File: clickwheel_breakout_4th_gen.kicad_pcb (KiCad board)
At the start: 2 copper layers, 55.5 x 98.2 mm, 7 parts, among them J1 SFV8R-2STE1HLF, J2 SFV14R-2STE1HLF, J3 SFV8R-2STE1HLF, J4 SFV14R-2STE1HLF, J5 Conn_02x08_Odd_Even, J6 Conn_02x14_Odd_Even, J7 USB_C_Receptacle_USB2.0

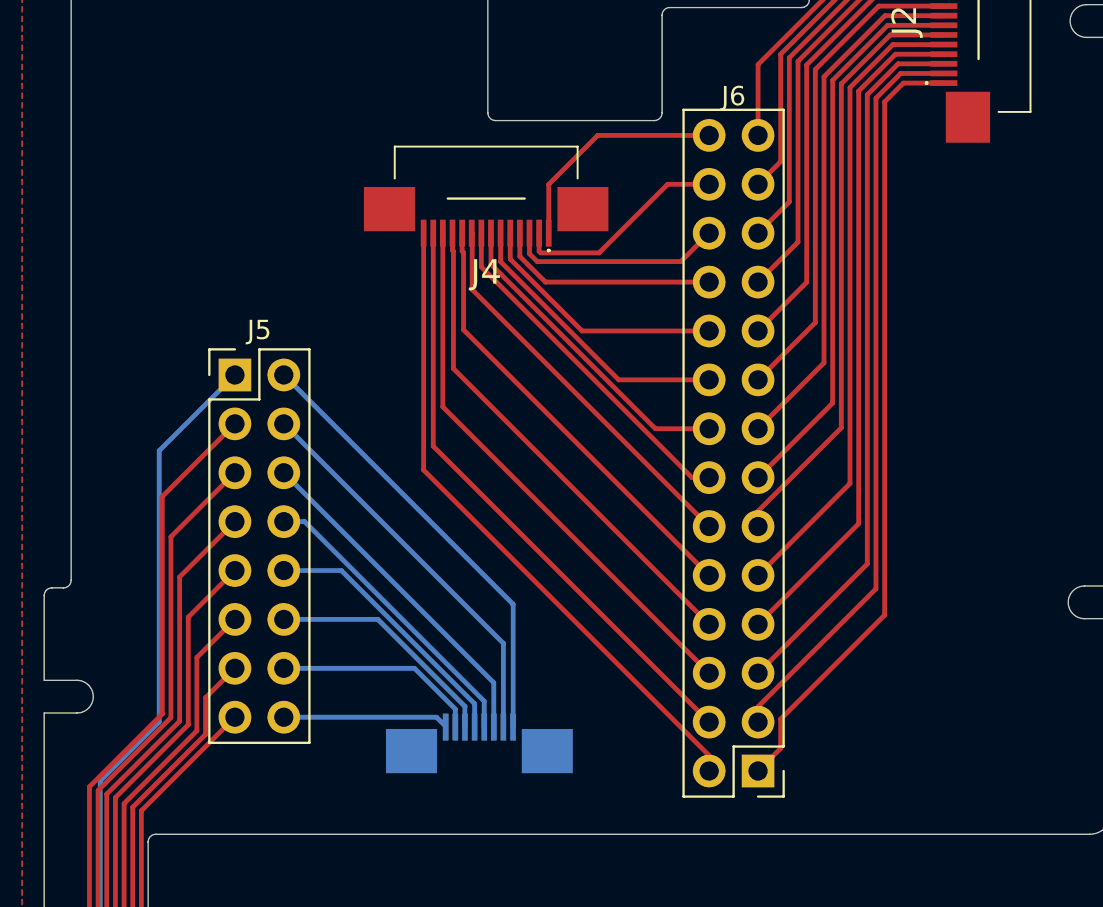
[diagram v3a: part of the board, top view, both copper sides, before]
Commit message: Add known headphone signal names with silkscreen
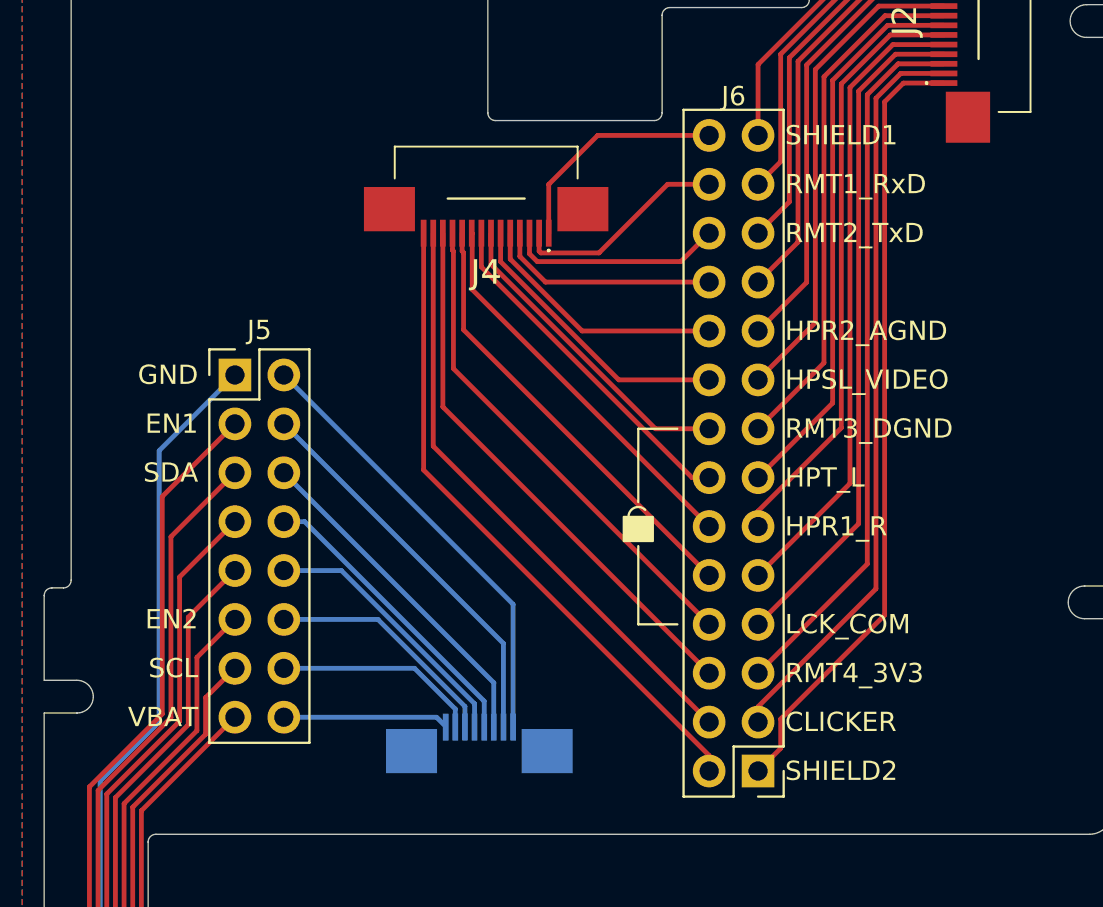
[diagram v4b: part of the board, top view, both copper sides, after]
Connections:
- net GND renamed Net-(J7-PadA1)
- net HP_1 renamed HP_SHIELD2
- net HP_10 renamed HP_HPR2_AGND
- net HP_10MB renamed HP_HPR2_AGNDMB
- net HP_12 renamed HP_RMT2_TxD
- net HP_12MB renamed HP_RMT2_TxDMB
- net HP_13 renamed HP_RMT1_RxD
- net HP_13MB renamed HP_RMT1_RxDMB
- net HP_14 renamed HP_SHIELD1
- net HP_14MB renamed HP_SHIELD1MB
- net HP_1MB renamed HP_SHIELD2MB
- net HP_2 renamed HP_CLICKER
- net HP_2MB renamed HP_CLICKERMB
- net HP_3 renamed HP_RMT4_3V3
- net HP_3MB renamed HP_RMT4_3V3MB
- net HP_4 renamed HP_LCK_COM
- net HP_4MB renamed HP_LCK_COMMB
- net HP_6 renamed HP_HPR1_R
- net HP_6MB renamed HP_HPR1_RMB
- net HP_7 renamed HP_HPT_L
- net HP_7MB renamed HP_HPT_LMB
- net HP_8 renamed HP_RMT3_DGND
- net HP_8MB renamed HP_RMT3_DGNDMB
- net HP_9 renamed HP_HPSL_VIDEO
- net HP_9MB renamed HP_HPSL_VIDEOMB
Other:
- board text added: "CLICKER"
- board text added: "Connect LCK_COM to DGND to unlock controls"
- board text added: "HPR1_R"
- board text added: "HPR2_AGND"
- board text added: "HPSL_VIDEO"
- board text added: "HPT_L"
- board text added: "LCK_COM"
- board text added: "RMT1_RxD"
- board text added: "RMT2_TxD"
- board text added: "RMT3_DGND"
- board text added: "RMT4_3V3"
- board text added: "SHIELD1"
- board text added: "SHIELD2"

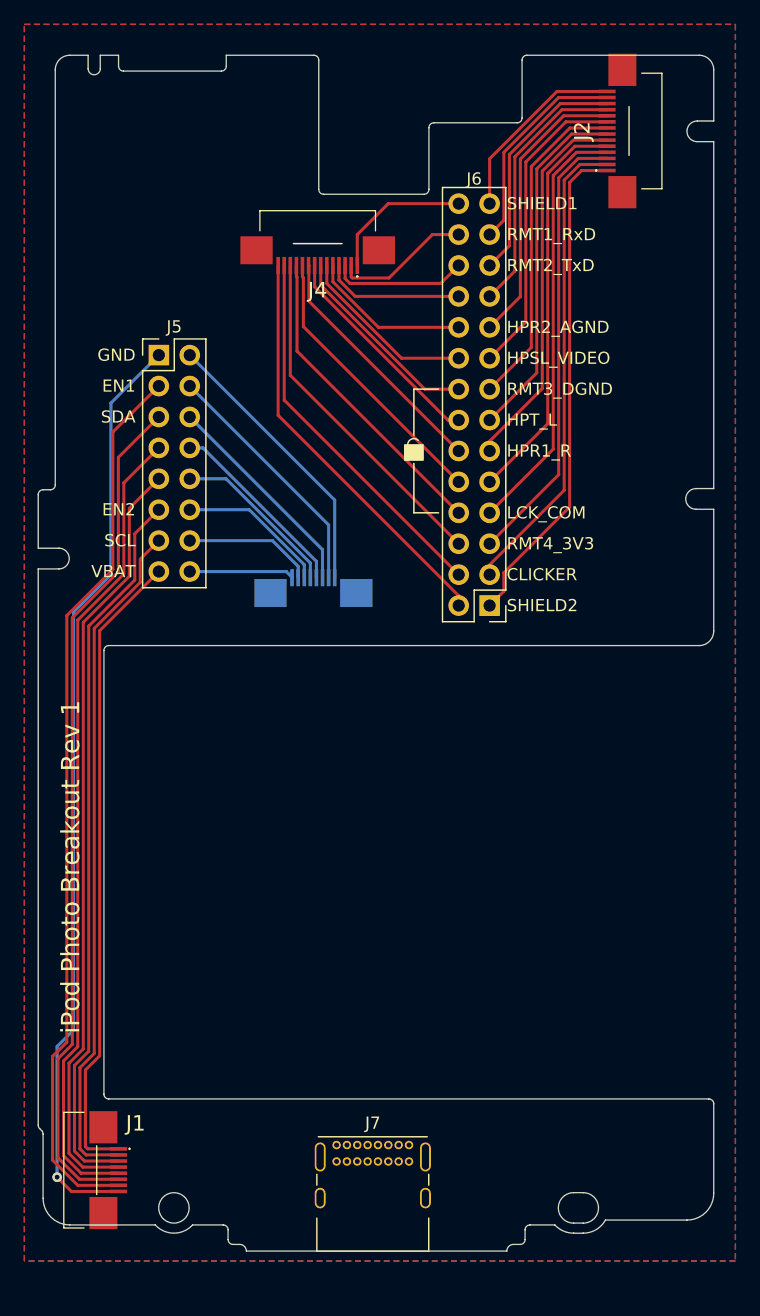
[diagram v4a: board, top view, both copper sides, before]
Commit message: kicad: update to kicad 6
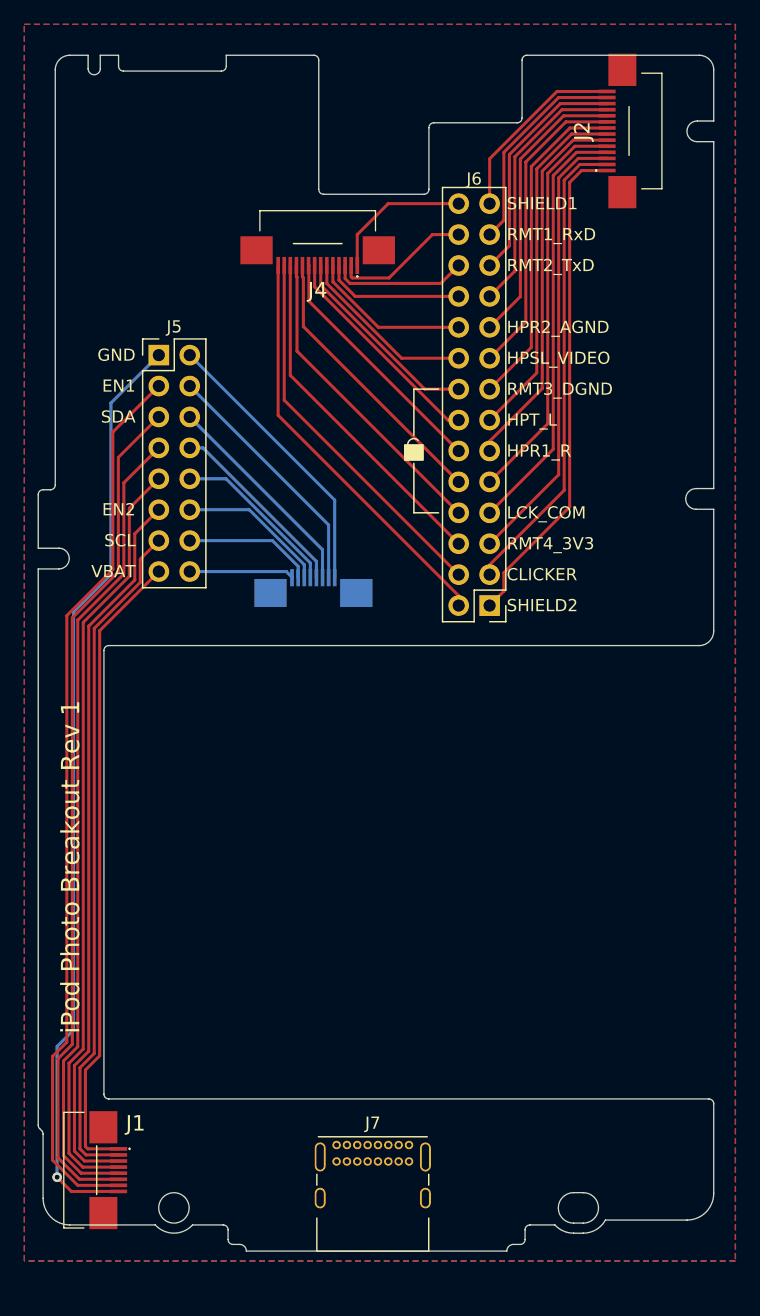
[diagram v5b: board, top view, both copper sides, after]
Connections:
- J1 pad M1: Net-(J1-PadM1) -> unconnected-(J1-PadM1)
- J1 pad M2: Net-(J1-PadM2) -> unconnected-(J1-PadM2)
- J2 pad M1: Net-(J2-PadM1) -> unconnected-(J2-PadM1)
- J2 pad M2: Net-(J2-PadM2) -> unconnected-(J2-PadM2)
- J3 pad M1: Net-(J3-PadM1) -> unconnected-(J3-PadM1)
- J3 pad M2: Net-(J3-PadM2) -> unconnected-(J3-PadM2)
- J4 pad M1: Net-(J4-PadM1) -> unconnected-(J4-PadM1)
- J4 pad M2: Net-(J4-PadM2) -> unconnected-(J4-PadM2)
- J7 pad A1: Net-(J7-PadA1) -> unconnected-(J7-PadA1)
- J7 pad A12: Net-(J7-PadA1) -> unconnected-(J7-PadA1)
- J7 pad A4: Net-(J7-PadA4) -> unconnected-(J7-PadA4)
- J7 pad A5: Net-(J7-PadA5) -> unconnected-(J7-PadA5)
- J7 pad A6: Net-(J7-PadA6) -> unconnected-(J7-PadA6)
- J7 pad A7: Net-(J7-PadA7) -> unconnected-(J7-PadA7)
- J7 pad A8: Net-(J7-PadA8) -> unconnected-(J7-PadA8)
- J7 pad A9: Net-(J7-PadA4) -> unconnected-(J7-PadA4)
- J7 pad B1: Net-(J7-PadA1) -> unconnected-(J7-PadA1)
- J7 pad B12: Net-(J7-PadA1) -> unconnected-(J7-PadA1)
- J7 pad B4: Net-(J7-PadA4) -> unconnected-(J7-PadA4)
- J7 pad B5: Net-(J7-PadB5) -> unconnected-(J7-PadB5)
- J7 pad B6: Net-(J7-PadB6) -> unconnected-(J7-PadB6)
- J7 pad B7: Net-(J7-PadB7) -> unconnected-(J7-PadB7)
- J7 pad B8: Net-(J7-PadB8) -> unconnected-(J7-PadB8)
- J7 pad B9: Net-(J7-PadA4) -> unconnected-(J7-PadA4)
- J7 pad S1: Net-(J7-PadS1) -> unconnected-(J7-PadS1)
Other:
- outline, holes or cut-outs redrawn
- net class Default removed

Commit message: kibot: add initial generated QR code
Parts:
- added QR1: QR_data, clickwheel_breakout_4th_gen-qr:QR_data, B.Cu at (63.1, 66.6)

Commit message: ci: add CI (#1)
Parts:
- QR1: footprint clickwheel_breakout_4th_gen-qr:QR_data -> QR:QR_data; moved to F.Cu
- moved QR1 5.50 mm to (61.8, 71.9), turned to 0 degrees

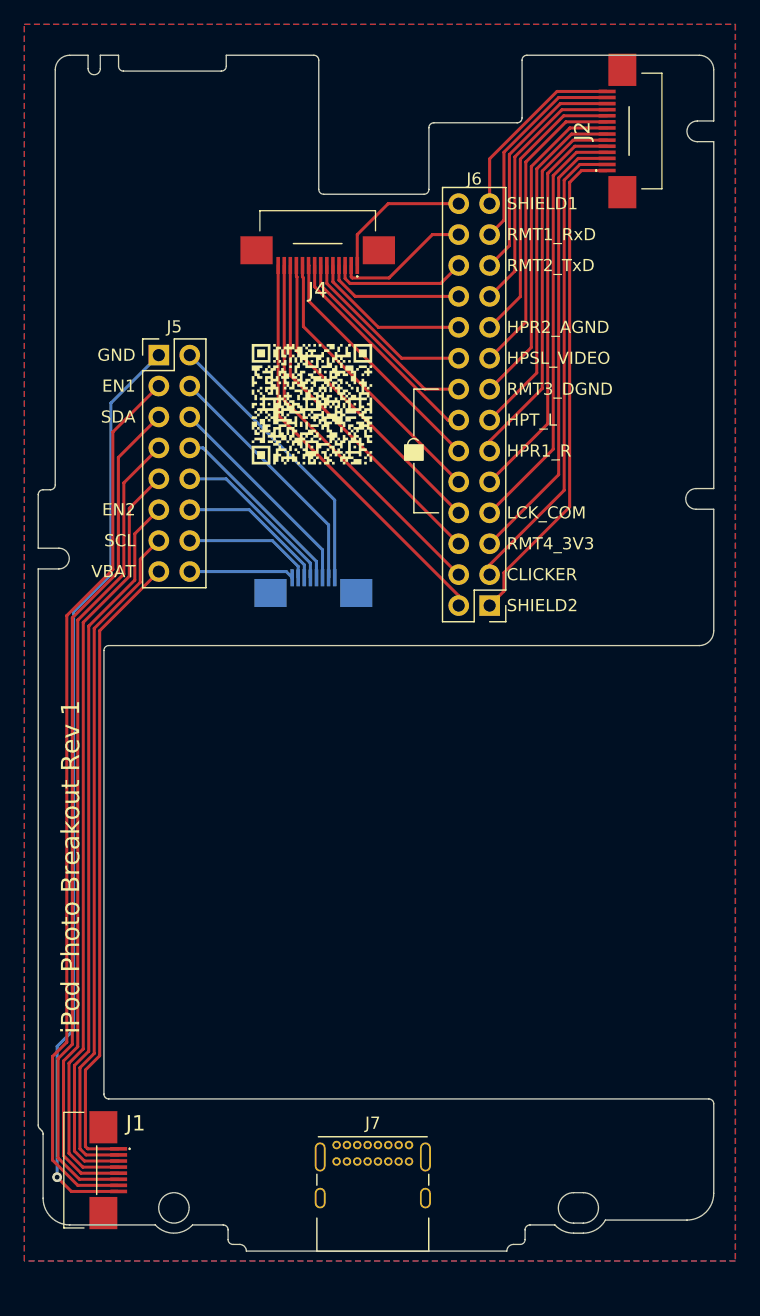
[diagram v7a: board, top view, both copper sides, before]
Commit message: silkscreen: add label for missing headphone AGND
- silkscreen: add connection instructions
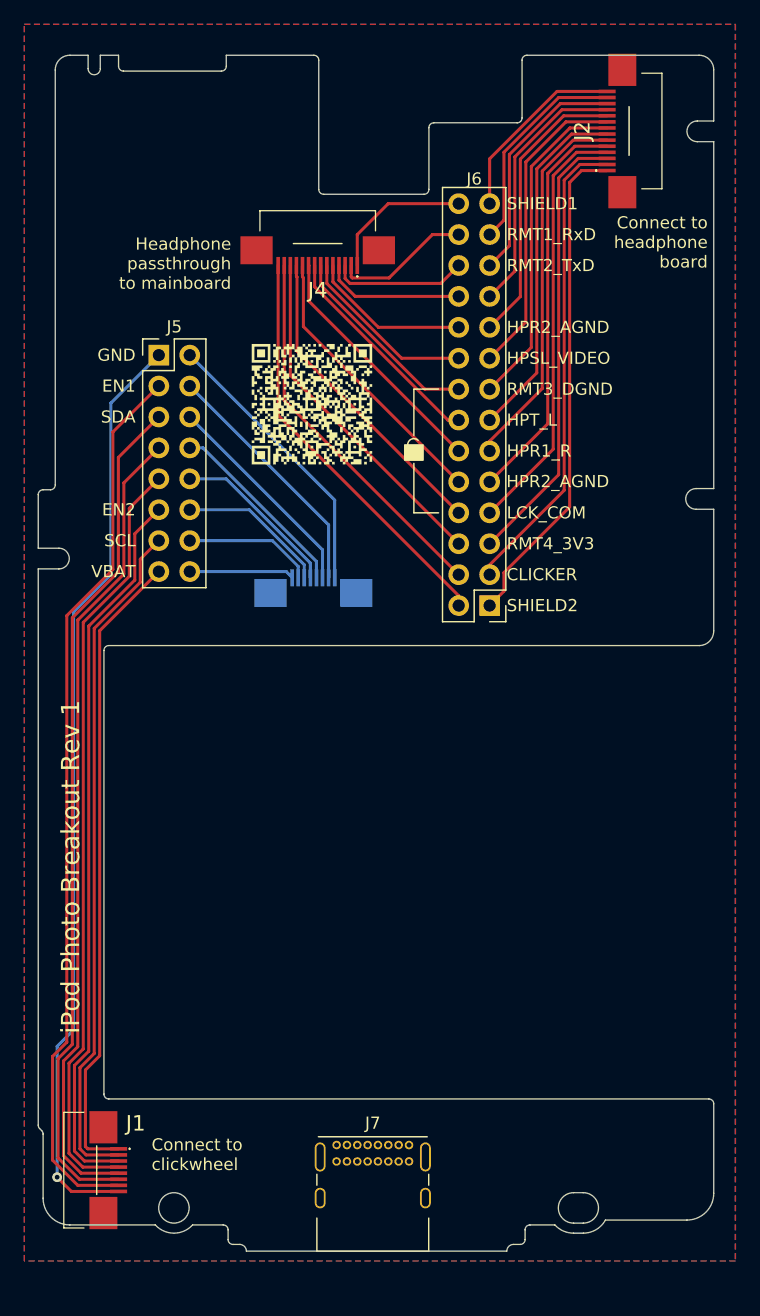
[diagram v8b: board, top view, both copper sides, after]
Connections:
- net HP_5 renamed HP_HPR2_AGND#2
- net HP_5MB renamed HP_HPR2_AGNDMB#2
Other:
- board text added: "Clickwheel passthrough to mainboard"
- board text added: "Connect to clickwheel"
- board text added: "Connect to headphone board"
- board text added: "Headphone passthrough to mainboard"
